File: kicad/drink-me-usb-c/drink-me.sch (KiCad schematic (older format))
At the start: 22 parts, among them J0 AVR-ISP-6, J1 USB4105_REVA, K0 KEYSW, K1 KEYSW, K2 KEYSW, K3 KEYSW, SW1 RESET, U1 32U2-AU, Y1 16Mhz

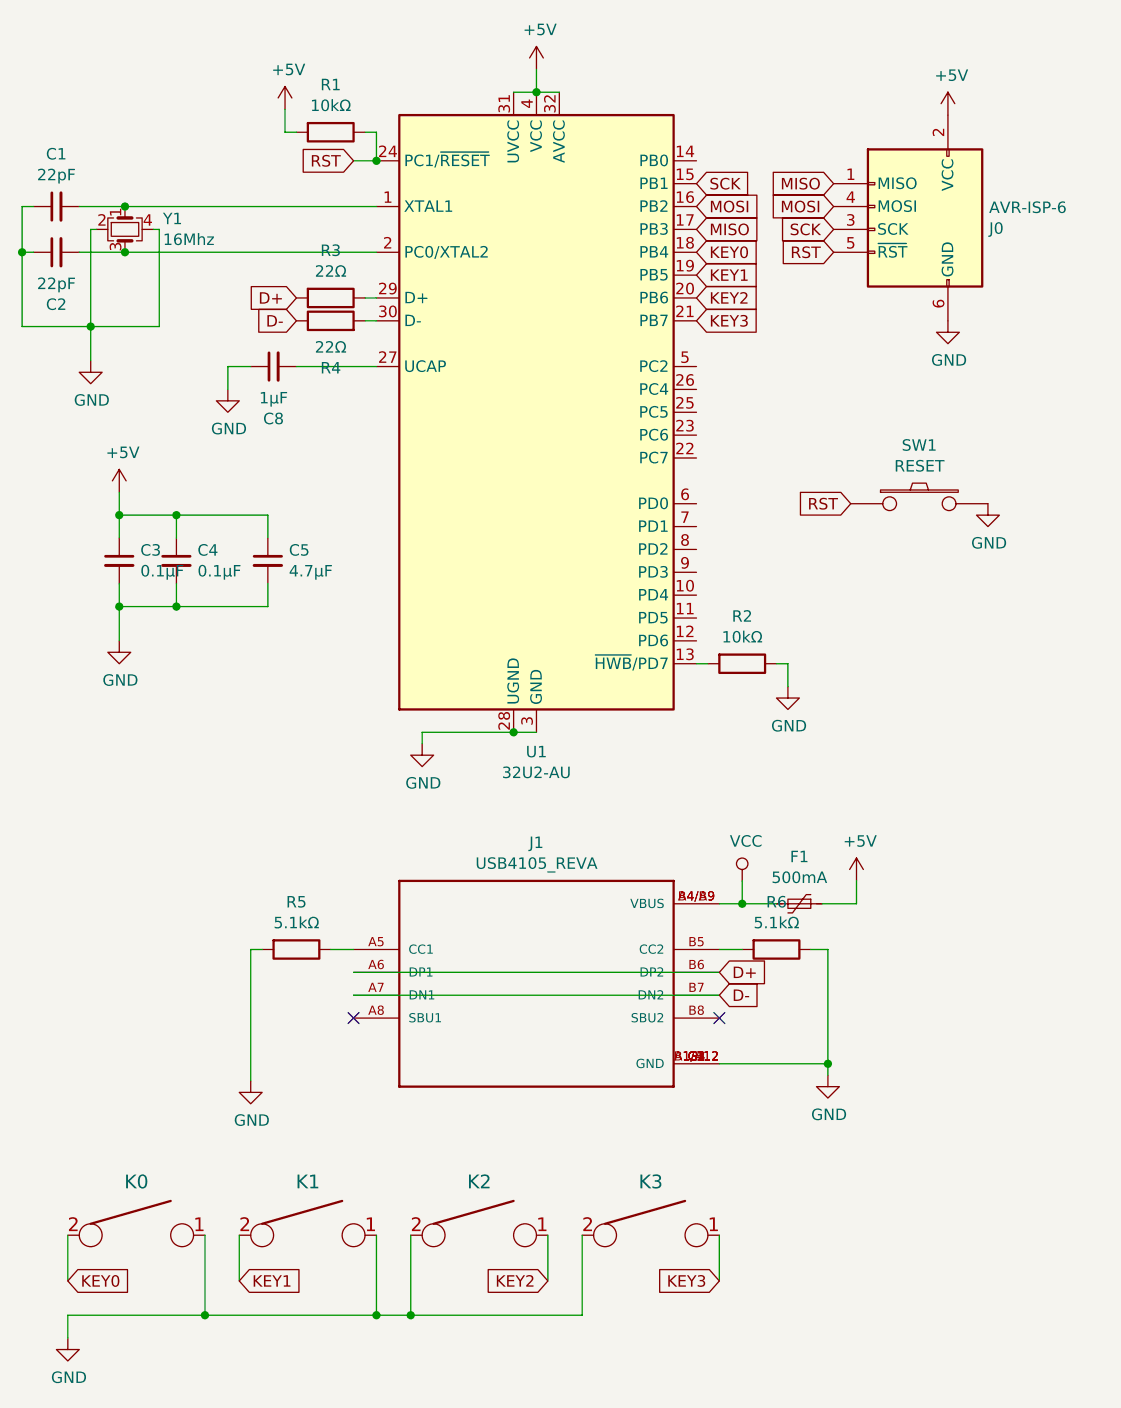
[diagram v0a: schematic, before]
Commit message: Use HRO TYPE-C-31-M-12 USB-C connector. Add bill of materials. Add printed back part without rest, including tolerance adjustments.
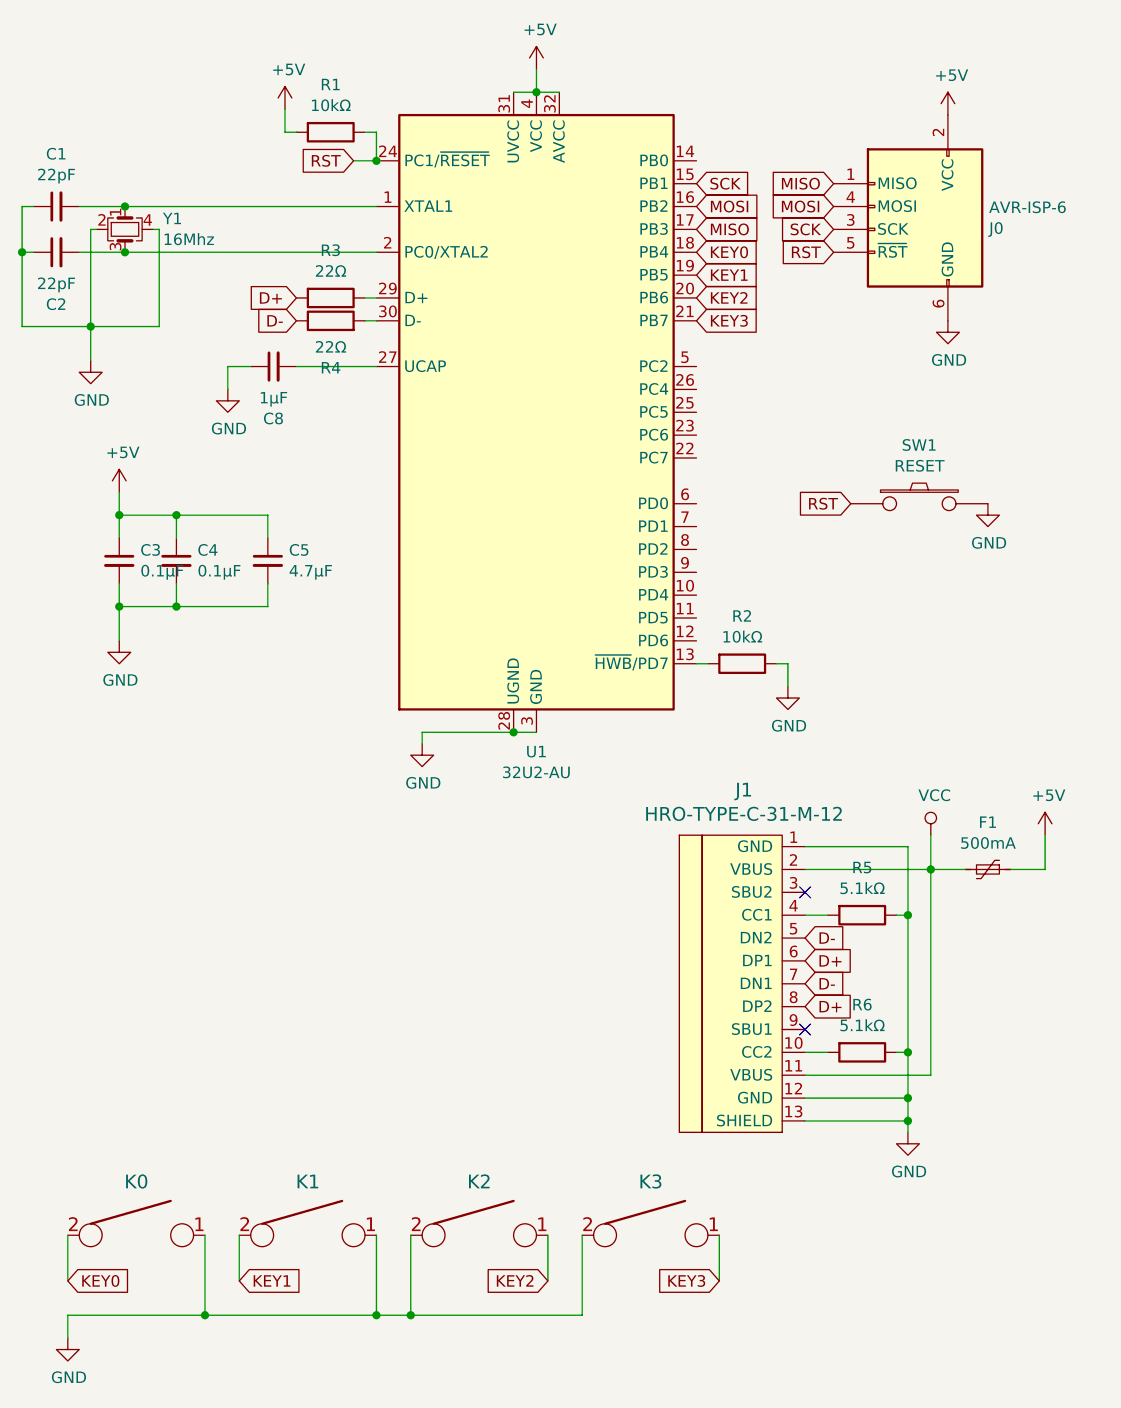
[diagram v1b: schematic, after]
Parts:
- removed J1: USB4105_REVA, SnapEDA:GCT_USB4105_REVA, symbol USB4105_REVA:USB4105_REVA
- added J1: HRO-TYPE-C-31-M-12, Type-C:HRO-TYPE-C-31-M-12-Assembly, symbol Type-C:HRO-TYPE-C-31-M-12
- C1, C2: BomReferenceDigiKey (none) -> 311-1103-1-ND; ComponentStencilOpenSCAD (none) -> csquare([2, 1.2]);
- C3, C4: BomReferenceDigiKey (none) -> 311-1361-1-ND; ComponentStencilOpenSCAD (none) -> csquare([2, 1.2]);
- C5: BomReferenceDigiKey (none) -> 311-1371-1-ND; ComponentStencilOpenSCAD (none) -> csquare([2, 1.2]);
- C8: BomReferenceDigiKey (none) -> 311-1909-1-ND; ComponentStencilOpenSCAD (none) -> csquare([2, 1.2]);
- F1: BomReferenceDigiKey (none) -> 0ZCJ0050AF2E; ComponentStencilOpenSCAD (none) -> csquare([3.2, 1.6]);
- K0, K1, K2, K3: ComponentStencilOpenSCAD (none) -> translate([0.635, -3.81]) csquare([14.5, 5.9]);
- R1, R2: BomReferenceDigiKey (none) -> CR0805-JW-103ELFCT-ND; ComponentStencilOpenSCAD (none) -> csquare([2, 1.2]);
- R3, R4: BomReferenceDigiKey (none) -> 118-CR0805-JW-220ELFCT-ND; ComponentStencilOpenSCAD (none) -> csquare([2, 1.2]);
- R5, R6: BomReferenceDigiKey (none) -> 118-CR0805-JW-512ELFCT-ND; ComponentStencilOpenSCAD (none) -> csquare([2, 1.2]);
- SW1: BomReferenceDigiKey (none) -> EG5470CT-ND; ComponentStencilOpenSCAD (none) -> csquare([6.6, 5.1]);
- U1: BomReferenceDigiKey (none) -> ATMEGA32U2-AURCT-ND; ComponentStencilOpenSCAD (none) -> csquare([9.2, 9.2]);
- Y1: BomReferenceDigiKey (none) -> SER3686CT-ND; ComponentStencilOpenSCAD (none) -> csquare([3.2, 2.5]);
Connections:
- net D+: now also J1.6 (DP1), J1.8 (DP2)
- net D-: now also J1.5 (DN2), J1.7 (DN1)
- net GND: now also R5.1, J1.1 (GND), J1.12 (GND), J1.13 (SHIELD); no longer R5.2
- net VCC: now also J1.11 (VBUS), J1.2 (VBUS)
- net at R6.2: now also J1.10 (CC2)
- new net: J1.4 (CC1), R5.2
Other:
- moved on the sheet: F1, R5, R6
